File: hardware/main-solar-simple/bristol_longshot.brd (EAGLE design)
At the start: 14 x 64 mm, 65 parts, among them U1 SAM_D20E, U2 SI4060, U3 UBLOX_MAX, U4 SST25WF040BT-40I/NP, U5 TG-5006CJ, U6 LTC3105EDDPBF, U7 TPS3123, U8 SN74LVC1G32DCKR, U9 BMP180

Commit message: Updated schematic labels, fixed R11 value
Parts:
- R11: value 86kΩ -> 68kΩ
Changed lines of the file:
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@@
 <element name="U4" library="fbri" package="USON-8" value="SST25WF040BT-40I/NP" x="3" y="20.125"/>
 <element name="R12" library="microbuilder_v3" package="_0402" value="82kΩ" x="2.25" y="33.875" rot="R270"/>
-<element name="R11" library="microbuilder_v3" package="_0402" value="86kΩ" x="2.25" y="32" rot="R270"/>
+<element name="R11" library="microbuilder_v3" package="_0402" value="68kΩ" x="2.25" y="32" rot="R270"/>
 <element name="C34" library="microbuilder_v3" package="_0402" value="1µF" x="2.25" y="35.875" rot="R270"/>
 <element name="C27" library="microbuilder_v3" package="_0402" value="4.7µF" x="3.5" y="31.25" rot="R270"/>

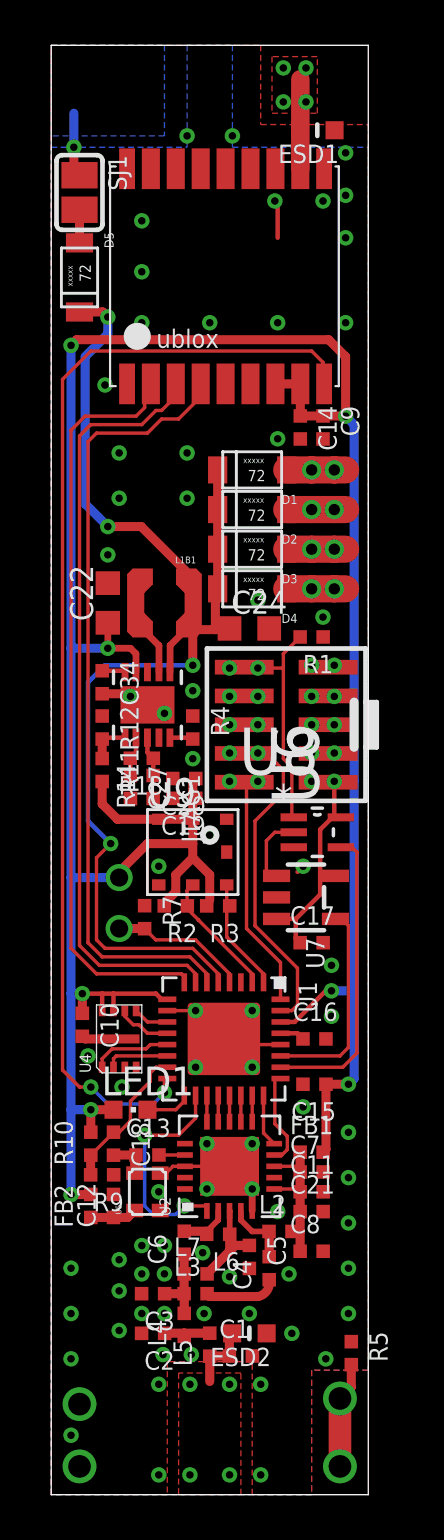
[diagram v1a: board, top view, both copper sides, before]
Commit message: Parts list complete for main-solar-simple (v0.985)
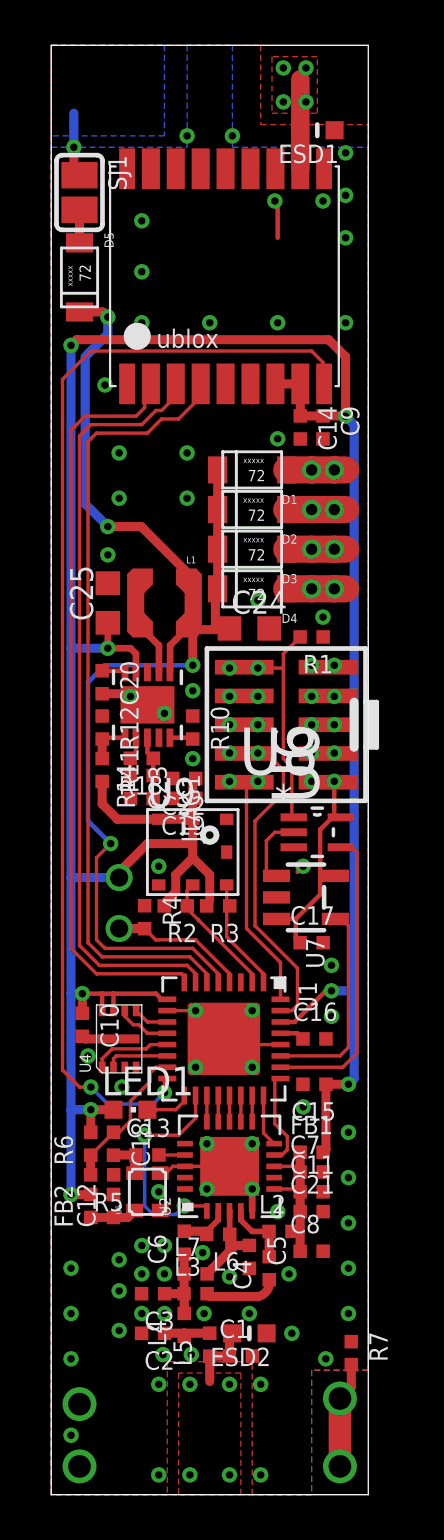
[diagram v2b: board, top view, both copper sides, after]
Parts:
- removed C34: 1µF, microbuilder_v3:_0402
- removed R9: 100kΩ, microbuilder_v3:_0402
- added C25: 10µF, resistor:C0603K
- added R6: 100kΩ, microbuilder_v3:_0402
- C20: value 4.7µF -> 1µF
- C22: value 10µF -> 4.7µF; device resistor:C0603K -> microbuilder_v3:_0402
- R10: value 100kΩ -> 82kΩ
- R4: value 82kΩ -> 100kΩ
- R5: value 0Ω -> 100kΩ
- R7: value 100kΩ -> 0Ω
- moved R7 21.3 mm to (13.2, 6.25)
- moved R10 18.9 mm to (6.25, 33.9), turned to 270 degrees
- moved R5 13.5 mm to (2.25, 14.1), turned to 180 degrees
- moved R4 8.64 mm to (4.12, 25.5)
- moved C22 8.45 mm to (5.88, 31.6), turned to 180 degrees
- moved C20 5.59 mm to (2.25, 35.9), turned to 270 degrees
- renumbered C27 to C23, L1B1 to L1
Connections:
- net 1.8V: now also C25.1, R6.2; no longer C20.1, R10.2
- net EXT_THERMISTOR_SENSE: now also R4.2; no longer R7.2
- net GND: now also C25.2, R10.1; no longer C34.2, R9.1
- net MPPT_AUX: now also C20.1; no longer C34.1
- net MPPT_SET: now also R10.2; no longer R4.2
- net SAM_XOSC: now also R5.2, R6.1; no longer R10.1, R9.2
- net SOLAR_MID: now also R7.2; no longer R5.2

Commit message: Final board changes for solar/primary lithium AAA (v0.985.0)
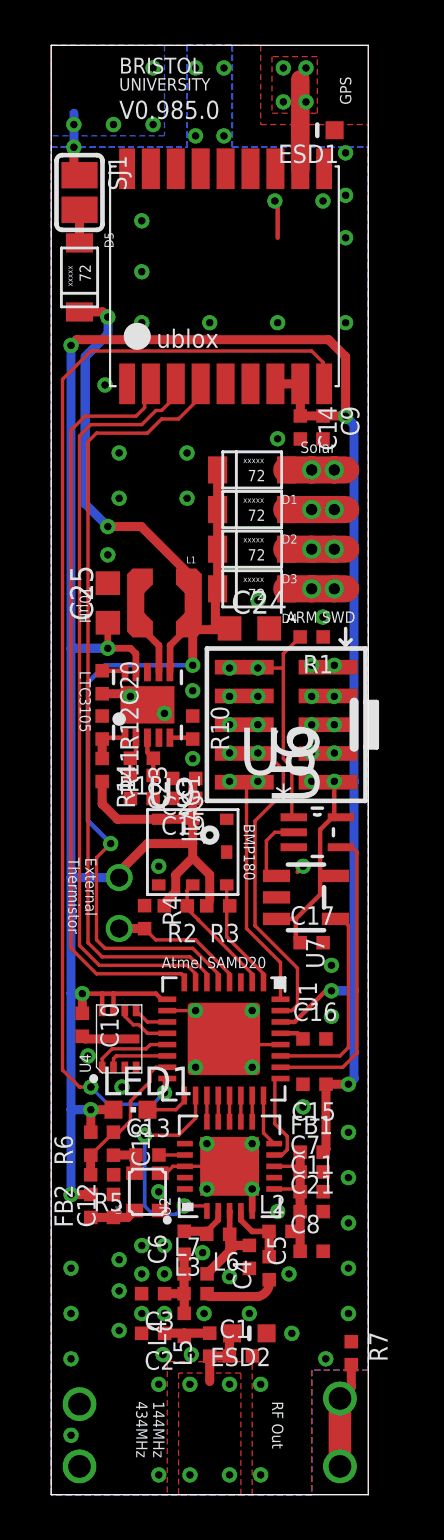
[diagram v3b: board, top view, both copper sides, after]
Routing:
- net PRIMARY_AAA_CONTACT: vias 1 -> 5
- net GND: vias 81 -> 83

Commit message: Added DNP/0Ω for when using battery only on main-solar-simple
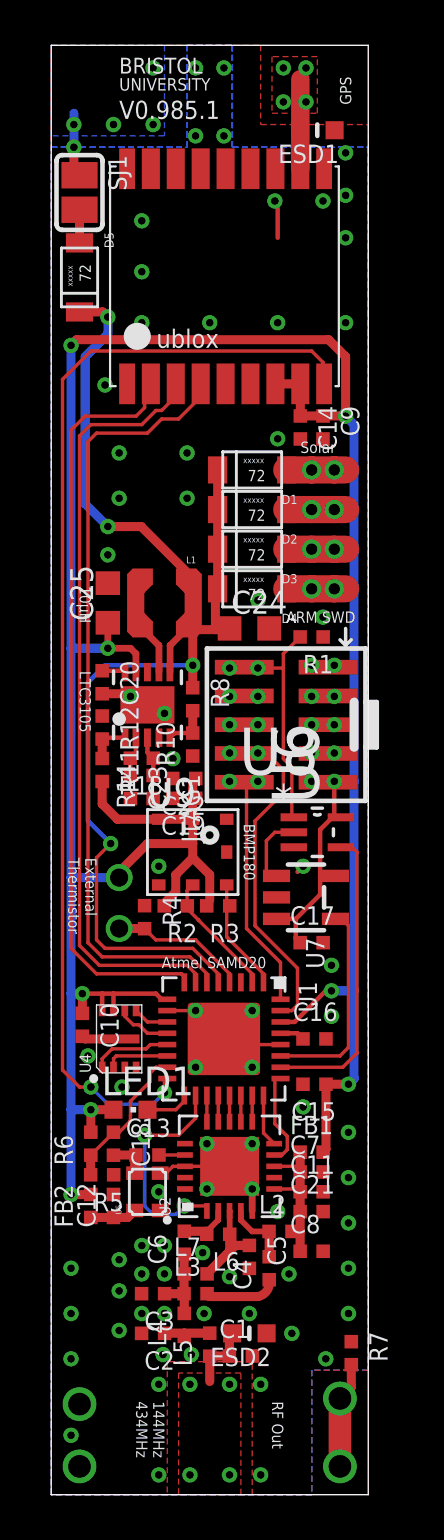
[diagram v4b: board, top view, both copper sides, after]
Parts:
- added R8: DNP, microbuilder_v3:_0402
- moved R10 0.75 mm to (6.25, 33.1), turned to 90 degrees
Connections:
- net MPPT_SET: now also R8.2
- net SOLAR: now also R8.1
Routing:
- net MPPT_SET: track 1.03 -> 2.08 mm
- net SOLAR: track 57.8 -> 58.8 mm
- net GND: vias 83 -> 82
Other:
- board text added: "V0.985.1"
- board text removed: "V0.985.0"
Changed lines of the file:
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@@
 <rectangle x1="5.5" y1="0.25" x2="8.5" y2="5.5" layer="29"/>
 <rectangle x1="9.625" y1="59.875" x2="11.875" y2="63.625" layer="29"/>
-<text x="3" y="60.75" size="0.8" layer="21" font="vector" ratio="14">V0.985.0</text>
+<text x="3" y="60.75" size="0.8" layer="21" font="vector" ratio="14">V0.985.1</text>
 <polygon width="0.2" layer="29">
 <vertex x="0.375" y="4.75"/>
@@
 <element name="D1" library="RB161M" package="RB161M" value="RB161M" x="8.875" y="45.25" rot="R90"/>
 <element name="L1" library="PecanFemto4" package="LPS3015" value="10uH LPS3015" x="5" y="39.375" rot="R180"/>
-<element name="R10" library="microbuilder_v3" package="_0402" value="82kΩ" x="6.25" y="33.875" rot="R270"/>
+<element name="R10" library="microbuilder_v3" package="_0402" value="82kΩ" x="6.25" y="33.125" rot="R90"/>
 <element name="C25" library="resistor" package="C0603K" value="10µF" x="2.5" y="39.375" rot="R90"/>
 <element name="D4" library="RB161M" package="RB161M" value="RB161M" x="8.875" y="40" rot="R90"/>
@@
 <element name="SJ1" library="microbuilder_v3" package="SOLDERJUMPER_REFLOW" value="" x="1.25" y="57.5" rot="R270"/>
 <element name="R7" library="microbuilder_v3" package="_0402" value="0Ω" x="13.25" y="6.25" rot="R270"/>
+<element name="R8" library="microbuilder_v3" package="_0402" value="DNP" x="6.25" y="35.125" rot="R270"/>
 </elements>
 <signals>
@@
 <wire x1="3.383" y1="35.367" x2="3.5" y2="35.25" width="0.4" layer="1"/>
 <via x="10" y="46.625" extent="1-16" drill="0.3302"/>
-<via x="6.25" y="35.5" extent="1-16" drill="0.3302"/>
 <via x="9.125" y="39.5" extent="1-16" drill="0.3302"/>
 <via x="12" y="38.75" extent="1-16" drill="0.3302"/>
@@
 <contactref element="R4" pad="1"/>
 <contactref element="R14" pad="1"/>
-<via x="6.25" y="32.5" extent="1-16" drill="0.3302"/>
+<via x="5.375" y="32.5" extent="1-16" drill="0.3302"/>
 <via x="2.5" y="41.5" extent="1-16" drill="0.3302"/>
 <via x="3" y="46" extent="1-16" drill="0.3302"/>
@@
 <wire x1="2.275" y1="52.225" x2="2.5" y2="52" width="0.4" layer="1"/>
 <wire x1="6.491484375" y1="38.197959375" x2="6.3977625" y2="38.1042375" width="0.2" layer="1"/>
+<contactref element="R8" pad="1"/>
+<wire x1="6.25" y1="35.633" x2="6.25" y2="36.625" width="0.4" layer="1"/>
 </signal>
 <signal name="PANEL_1">
@@
 <contactref element="U6" pad="5"/>
 <contactref element="R10" pad="2"/>
-<wire x1="5.2406" y1="33.4272" x2="6.1898" y2="33.4272" width="0.2" layer="1"/>
-<wire x1="6.1898" y1="33.4272" x2="6.25" y2="33.367" width="0.2" layer="1"/>
+<contactref element="R8" pad="2"/>
+<wire x1="6.25" y1="33.633" x2="6.25" y2="34.617" width="0.4" layer="1"/>
+<wire x1="5.2406" y1="33.4272" x2="5.4464" y2="33.633" width="0.2" layer="1"/>
+<wire x1="5.4464" y1="33.633" x2="6.25" y2="33.633" width="0.2" layer="1"/>
 </signal>
 <signal name="PANEL_4">

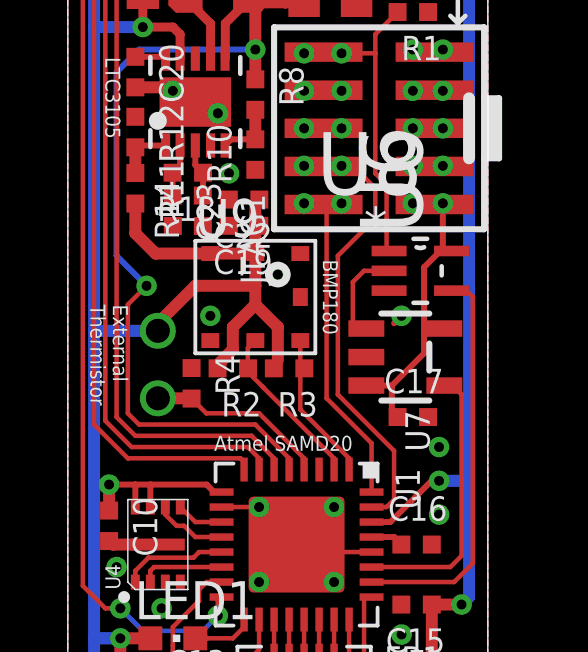
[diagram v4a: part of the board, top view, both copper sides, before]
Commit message: Hardware V0.985.2, replaces BMP180 with MS5607
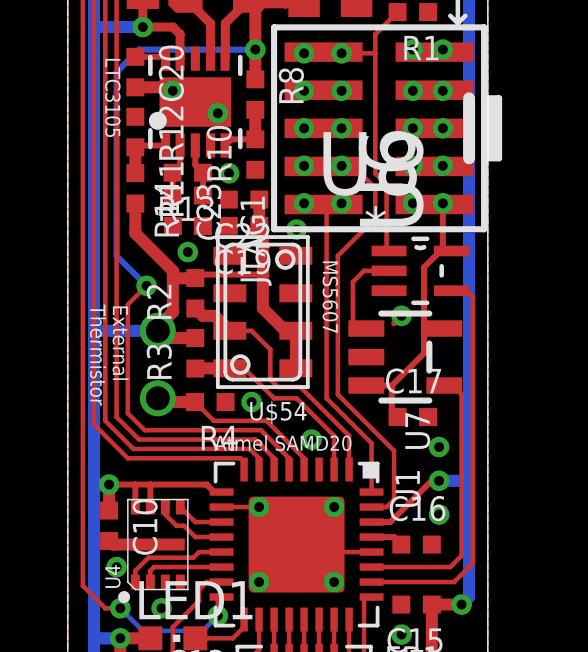
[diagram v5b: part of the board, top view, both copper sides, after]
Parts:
- removed U9: BMP180, SparkFun-Sensors:BMP180
- added U$54: MS5607-02BA03, MS5607-02BA03:MS5607-02BA03
- moved R3 3.16 mm to (4.25, 26.5), turned to 90 degrees
- moved R2 2.80 mm to (4.25, 28.5), turned to 90 degrees
- moved R4 0.88 mm to (4.75, 24.9), turned to 180 degrees
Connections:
- net 1.8V: now also U$54.1, U$54.2; no longer U9.2, U9.3
- net GND: now also U$54.3, U$54.4, U$54.5; no longer U9.7
- net SCL: now also R3.1, U$54.8; no longer R2.1, U9.5
- net SDA: now also R2.1, U$54.7; no longer R3.1, U9.6
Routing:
- net SDA: track 5.22 -> 8.59 mm
- net 1.8V: track 144.8 -> 142.7 mm
- net SCL: track 5.62 -> 6.69 mm
- net GND: vias 82 -> 84
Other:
- board text added: "MS5607"
- board text removed: "BMP180"

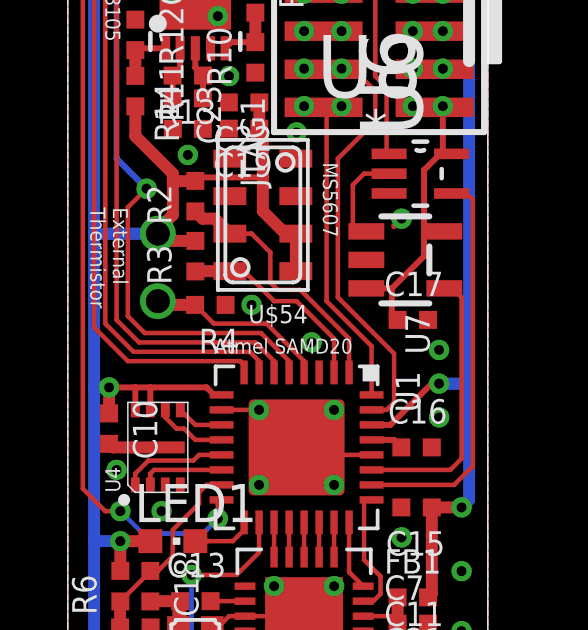
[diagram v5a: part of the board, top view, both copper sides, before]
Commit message: Update part name U9
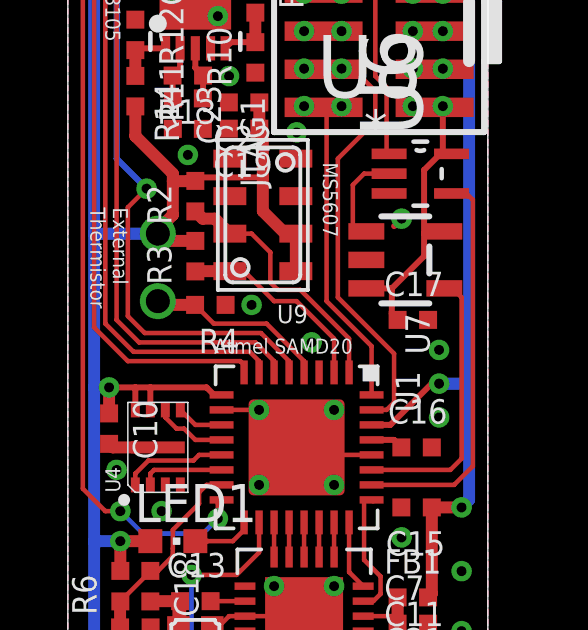
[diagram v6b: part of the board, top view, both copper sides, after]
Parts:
- renumbered U$54 to U9
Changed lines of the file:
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@@
 <element name="R7" library="microbuilder_v3" package="_0402" value="0Ω" x="13.25" y="6.25" rot="R270"/>
 <element name="R8" library="microbuilder_v3" package="_0402" value="DNP" x="6.25" y="35.125" rot="R270"/>
-<element name="U$54" library="MS5607-02BA03" package="MS5607-02BA03" value="MS5607-02BA03" x="6.5" y="27.875" rot="R180"/>
+<element name="U9" library="MS5607-02BA03" package="MS5607-02BA03" value="MS5607-02BA03" x="6.5" y="27.875" rot="R180"/>
 </elements>
 <signals>
@@
 </polygon>
 <via x="7.625" y="63" extent="1-16" drill="0.3302"/>
-<contactref element="U$54" pad="3"/>
+<contactref element="U9" pad="3"/>
 <contactref element="C19" pad="2"/>
-<contactref element="U$54" pad="5"/>
-<contactref element="U$54" pad="4"/>
+<contactref element="U9" pad="5"/>
+<contactref element="U9" pad="4"/>
 <via x="7.625" y="30.625" extent="1-16" drill="0.3302"/>
 <via x="6.125" y="24.875" extent="1-16" drill="0.3302"/>
@@
 <wire x1="2.5" y1="38.5" x2="2.5" y2="37.375" width="0.3" layer="1"/>
 <wire x1="2.5" y1="37.375" x2="0.875" y2="37.375" width="0.4" layer="16"/>
-<contactref element="U$54" pad="2"/>
+<contactref element="U9" pad="2"/>
 <wire x1="7.6" y1="27.25" x2="7.25" y2="27.25" width="0.4" layer="1"/>
 <wire x1="7.25" y1="27.25" x2="6.5" y2="28" width="0.4" layer="1"/>
@@
 <wire x1="4.25" y1="29.125" x2="4.25" y2="29.008" width="0.2" layer="1"/>
 <contactref element="C19" pad="1"/>
-<contactref element="U$54" pad="1"/>
+<contactref element="U9" pad="1"/>
 <contactref element="C22" pad="1"/>
 <wire x1="6.383" y1="31.625" x2="6.383" y2="30.75" width="0.4" layer="1"/>
@@
 <wire x1="9.375" y1="22.625" x2="9.375" y2="23.75" width="0.1524" layer="1"/>
 <wire x1="9.375" y1="23.75" x2="7.75" y2="25.375" width="0.1524" layer="1"/>
-<contactref element="U$54" pad="7"/>
+<contactref element="U9" pad="7"/>
 <contactref element="R2" pad="1"/>
 <wire x1="7.75" y1="25.375" x2="7" y2="25.375" width="0.1524" layer="1"/>
@@
 <signal name="SCL">
 <contactref element="U1" pad="2"/>
-<contactref element="U$54" pad="8"/>
+<contactref element="U9" pad="8"/>
 <contactref element="R3" pad="1"/>
 <wire x1="8.875" y1="22.625" x2="8.875" y2="23.75" width="0.1524" layer="1"/>
